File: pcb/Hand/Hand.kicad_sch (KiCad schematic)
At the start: 38 parts, among them J1 Conn_01x08_IMU_1, J10 Conn_01x03_HALL_7, J11 Conn_01x03_HALL_8, J12 Conn_01x03_HALL_9, J13 Conn_01x03_HALL_10, J14 Conn_01x03_HALL_11, J15 Conn_01x03_HALL_12, J16 Conn_01x03_HALL_13, J17 Conn_01x03_HALL_14, J18 Conn_01x03_HALL_15, J19 Conn_01x05_HAPTIC_1, J2 Conn_01x03_HALL_0, J20 Conn_01x05_HAPTIC_2, J21 Conn_01x05_HAPTIC_3, J22 Conn_01x05_HAPTIC_4, J23 Conn_01x03_FEEDBACK_0, J24 Conn_01x03_FEEDBACK_1, J25 Conn_01x03_FEEDBACK_2, J26 Conn_01x03_FEEDBACK_3, J27 Conn_01x03_FEEDBACK_4, J28 Conn_01x03_SPOOLPOT_1, J29 Conn_01x03_SPOOLPOT_2, J3 Conn_01x05_HAPTIC_0, J30 Conn_01x03_SPOOLPOT_3, J31 Conn_01x03_SPOOLPOT_0, J32 Conn_01x03_SPOOLPOT_4, J33 Conn_01x16_Ribbon_Bottom, J34 Conn_01x16_Ribbon_Top, J4 Conn_01x03_HALL_1, J5 Conn_01x03_HALL_2, J6 Conn_01x03_HALL_3, J7 Conn_01x03_HALL_4, J8 Conn_01x03_HALL_5, J9 Conn_01x03_HALL_6, U1 CD74HC4067M96, U3 TCA9548A

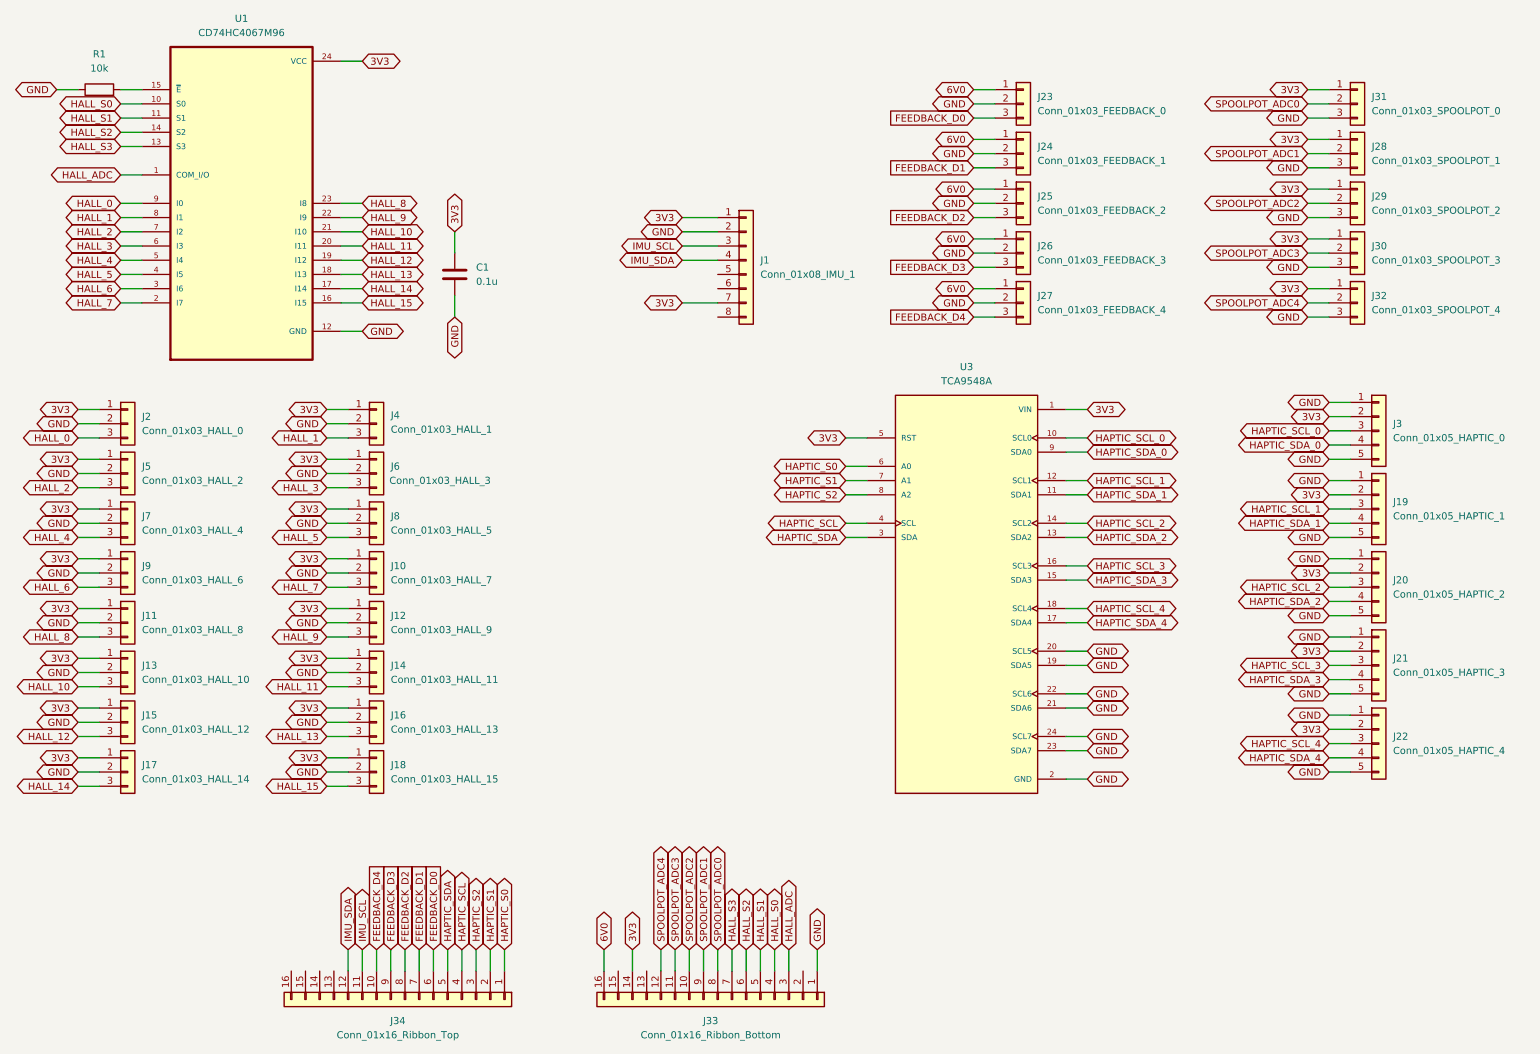
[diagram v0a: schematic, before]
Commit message: merging jackson pcb into main
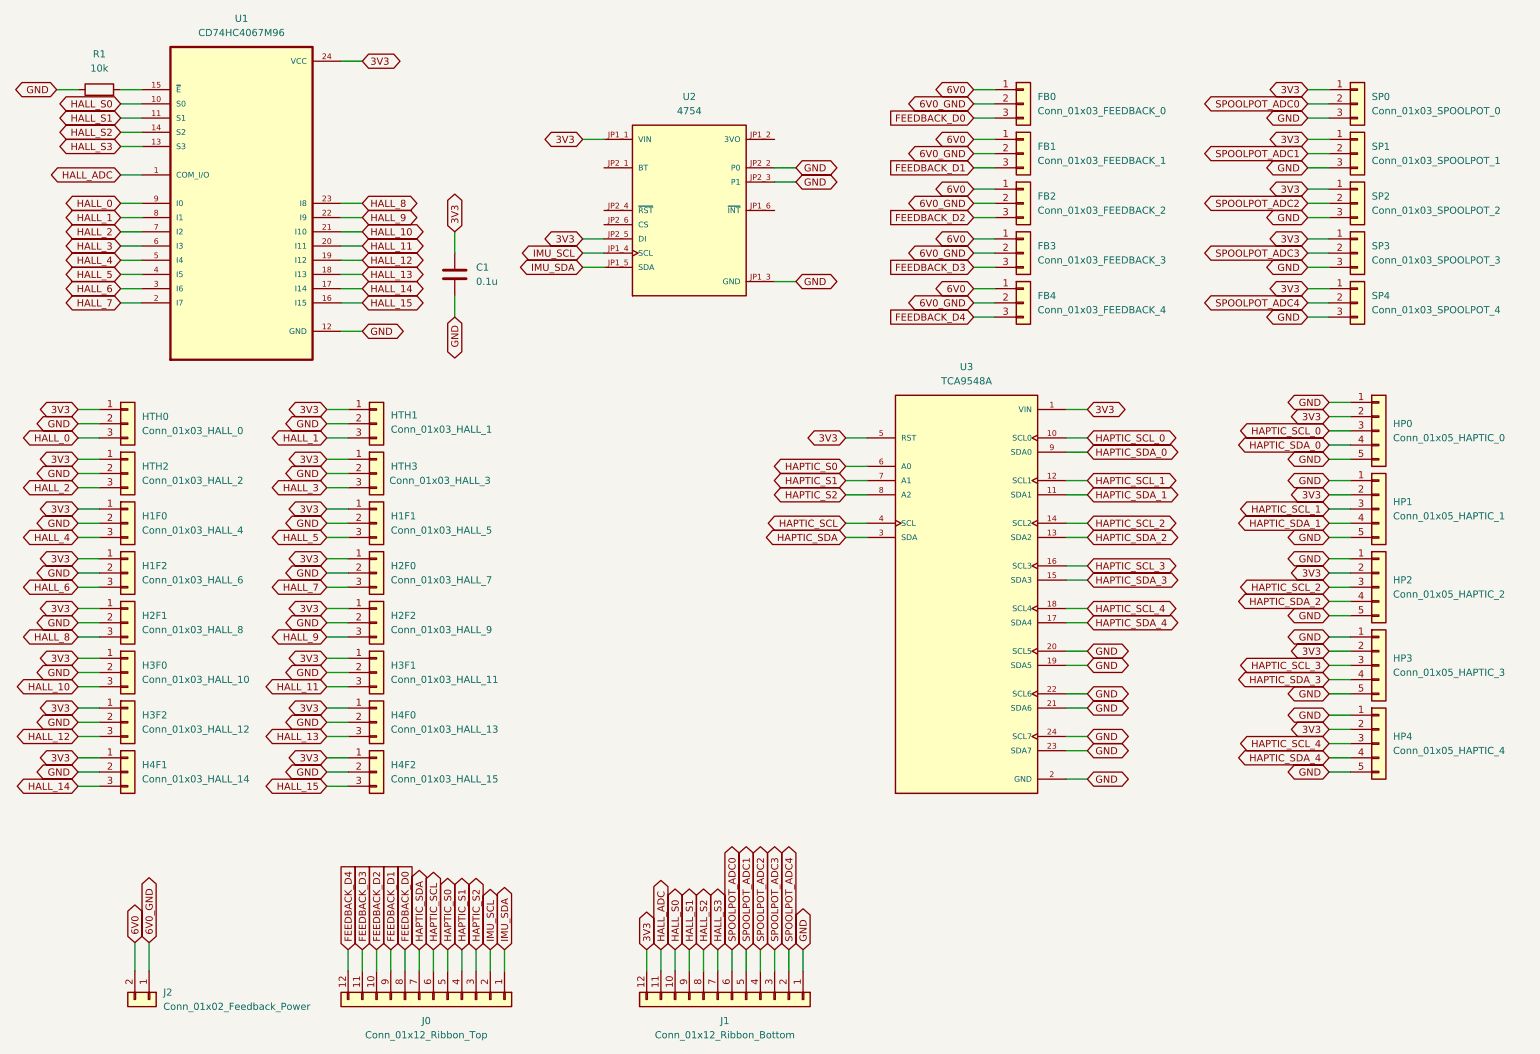
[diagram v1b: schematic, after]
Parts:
- removed J1: Conn_01x08_IMU_1, symbol Connector_Generic:Conn_01x08
- removed J33: Conn_01x16_Ribbon_Bottom, symbol Connector_Generic:Conn_01x16
- removed J34: Conn_01x16_Ribbon_Top, symbol Connector_Generic:Conn_01x16
- added J0: Conn_01x12_Ribbon_Top, 0522071233:0522071233, symbol Connector_Generic:Conn_01x12
- added J1: Conn_01x12_Ribbon_Bottom, 0522071233:0522071233, symbol Connector_Generic:Conn_01x12
- added J2: Conn_01x02_Feedback_Power, Connector_PinHeader_2.54mm:PinHeader_1x02_P2.54mm_Vertical, symbol Connector_Generic:Conn_01x02
- added U2: 4754, BNO085:MODULE_4754, symbol BNO085:4754
- C1: footprint (none) -> Capacitor_SMD:C_1206_3216Metric
- FB0: renamed from J23; footprint (none) -> SM03B-SRSS-TB:JST_SM03B-SRSS-TB_LF__SN_
- FB1: renamed from J24; footprint (none) -> SM03B-SRSS-TB:JST_SM03B-SRSS-TB_LF__SN_
- FB2: renamed from J25; footprint (none) -> SM03B-SRSS-TB:JST_SM03B-SRSS-TB_LF__SN_
- FB3: renamed from J26; footprint (none) -> SM03B-SRSS-TB:JST_SM03B-SRSS-TB_LF__SN_
- FB4: renamed from J27; footprint (none) -> SM03B-SRSS-TB:JST_SM03B-SRSS-TB_LF__SN_
- H1F0: renamed from J7; footprint (none) -> SM03B-SRSS-TB:JST_SM03B-SRSS-TB_LF__SN_
- H1F1: renamed from J8; footprint (none) -> SM03B-SRSS-TB:JST_SM03B-SRSS-TB_LF__SN_
- H1F2: renamed from J9; footprint (none) -> SM03B-SRSS-TB:JST_SM03B-SRSS-TB_LF__SN_
- H2F0: renamed from J10; footprint (none) -> SM03B-SRSS-TB:JST_SM03B-SRSS-TB_LF__SN_
- H2F1: renamed from J11; footprint (none) -> SM03B-SRSS-TB:JST_SM03B-SRSS-TB_LF__SN_
- H2F2: renamed from J12; footprint (none) -> SM03B-SRSS-TB:JST_SM03B-SRSS-TB_LF__SN_
- H3F0: renamed from J13; footprint (none) -> SM03B-SRSS-TB:JST_SM03B-SRSS-TB_LF__SN_
- H3F1: renamed from J14; footprint (none) -> SM03B-SRSS-TB:JST_SM03B-SRSS-TB_LF__SN_
- H3F2: renamed from J15; footprint (none) -> SM03B-SRSS-TB:JST_SM03B-SRSS-TB_LF__SN_
- H4F0: renamed from J16; footprint (none) -> SM03B-SRSS-TB:JST_SM03B-SRSS-TB_LF__SN_
- H4F1: renamed from J17; footprint (none) -> SM03B-SRSS-TB:JST_SM03B-SRSS-TB_LF__SN_
- H4F2: renamed from J18; footprint (none) -> SM03B-SRSS-TB:JST_SM03B-SRSS-TB_LF__SN_
- HP0: renamed from J3; footprint (none) -> SM05B-SRSS-TB:JST_SM05B-SRSS-TB_LF__SN_
- HP1: renamed from J19; footprint (none) -> SM05B-SRSS-TB:JST_SM05B-SRSS-TB_LF__SN_
- HP2: renamed from J20; footprint (none) -> SM05B-SRSS-TB:JST_SM05B-SRSS-TB_LF__SN_
- HP3: renamed from J21; footprint (none) -> SM05B-SRSS-TB:JST_SM05B-SRSS-TB_LF__SN_
- HP4: renamed from J22; footprint (none) -> SM05B-SRSS-TB:JST_SM05B-SRSS-TB_LF__SN_
- HTH0: renamed from J2; footprint (none) -> SM03B-SRSS-TB:JST_SM03B-SRSS-TB_LF__SN_
- HTH1: renamed from J4; footprint (none) -> SM03B-SRSS-TB:JST_SM03B-SRSS-TB_LF__SN_
- HTH2: renamed from J5; footprint (none) -> SM03B-SRSS-TB:JST_SM03B-SRSS-TB_LF__SN_
- HTH3: renamed from J6; footprint (none) -> SM03B-SRSS-TB:JST_SM03B-SRSS-TB_LF__SN_
- R1: footprint (none) -> Resistor_SMD:R_0402_1005Metric
- SP0: renamed from J31; footprint (none) -> SM03B-SRSS-TB:JST_SM03B-SRSS-TB_LF__SN_
- SP1: renamed from J28; footprint (none) -> SM03B-SRSS-TB:JST_SM03B-SRSS-TB_LF__SN_
- SP2: renamed from J29; footprint (none) -> SM03B-SRSS-TB:JST_SM03B-SRSS-TB_LF__SN_
- SP3: renamed from J30; footprint (none) -> SM03B-SRSS-TB:JST_SM03B-SRSS-TB_LF__SN_
- SP4: renamed from J32; footprint (none) -> SM03B-SRSS-TB:JST_SM03B-SRSS-TB_LF__SN_
- U3: footprint 2717:MODULE_2717 -> TCA9548A:MODULE_2717
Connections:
- net 3V3: now also J1.12 (Pin_12), U2.JP1_1 (VIN), U2.JP2_5 (DI)
- net 6V0: now also J2.2 (Pin_2)
- net FEEDBACK_D0: now also J0.8 (Pin_8)
- net FEEDBACK_D1: now also J0.9 (Pin_9)
- net FEEDBACK_D2: now also J0.10 (Pin_10)
- net FEEDBACK_D3: now also J0.11 (Pin_11)
- net FEEDBACK_D4: now also J0.12 (Pin_12)
- net GND: now also J1.1 (Pin_1), U2.JP1_3 (GND), U2.JP2_2 (P0), U2.JP2_3 (P1); no longer FB0.2 (Pin_2), FB1.2 (Pin_2), FB2.2 (Pin_2), FB3.2 (Pin_2), FB4.2 (Pin_2)
- net HALL_ADC: now also J1.11 (Pin_11)
- net HALL_S0: now also J1.10 (Pin_10)
- net HALL_S1: now also J1.9 (Pin_9)
- net HALL_S2: now also J1.8 (Pin_8)
- net HALL_S3: now also J1.7 (Pin_7)
- net HAPTIC_S0: now also J0.5 (Pin_5)
- net HAPTIC_S1: now also J0.4 (Pin_4)
- net HAPTIC_S2: now also J0.3 (Pin_3)
- net HAPTIC_SCL: now also J0.6 (Pin_6)
- net HAPTIC_SDA: now also J0.7 (Pin_7)
- net IMU_SCL: now also J0.2 (Pin_2), U2.JP1_4 (SCL)
- net IMU_SDA: now also J0.1 (Pin_1), U2.JP1_5 (SDA)
- net SPOOLPOT_ADC0: now also J1.6 (Pin_6)
- net SPOOLPOT_ADC1: now also J1.5 (Pin_5)
- net SPOOLPOT_ADC2: now also J1.4 (Pin_4)
- net SPOOLPOT_ADC3: now also J1.3 (Pin_3)
- net SPOOLPOT_ADC4: now also J1.2 (Pin_2)
- new net 6V0_GND: FB0.2 (Pin_2), FB1.2 (Pin_2), FB2.2 (Pin_2), FB3.2 (Pin_2), FB4.2 (Pin_2), J2.1 (Pin_1)

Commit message: revised pcbs in preparation for pcb review; added pull-ups etc to forearm
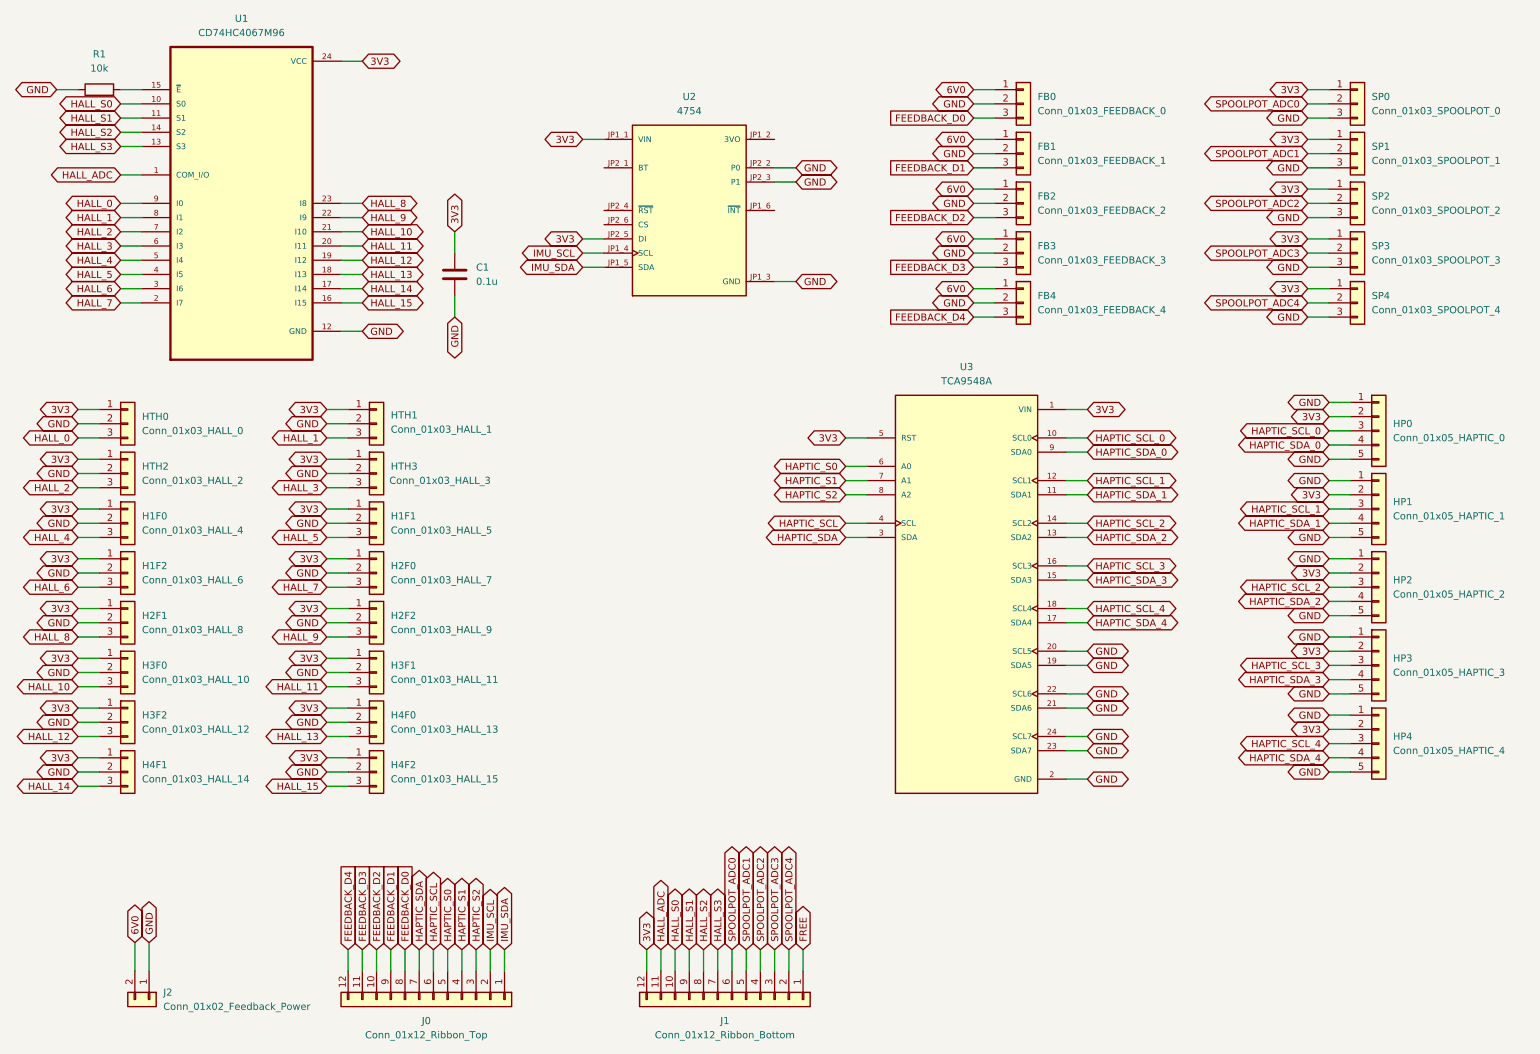
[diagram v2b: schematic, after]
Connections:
- net 6V0_GND is gone; now on net GND: FB0.2 (Pin_2), FB1.2 (Pin_2), FB2.2 (Pin_2), FB3.2 (Pin_2), FB4.2 (Pin_2), J2.1 (Pin_1)
- net GND: no longer J1.1 (Pin_1)
- new net FREE: J1.1 (Pin_1)
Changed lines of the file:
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@@
 	(global_label "GND"
 		(shape bidirectional)
+		(at 186.69 46.99 180)
+		(fields_autoplaced yes)
+		(effects
+			(font
+				(size 1.27 1.27)
+			)
+			(justify right)
+		)
+		(property "Intersheetrefs" "${INTERSHEET_REFS}"
+			(at 178.723 46.99 0)
+			(effects
+				(font
+					(size 1.27 1.27)
+				)
+				(justify right)
+				(hide yes)
+			)
+		)
+	)
+	(global_label "GND"
+		(shape bidirectional)
 		(at 71.12 148.59 180)
 		(fields_autoplaced yes)
@@
 		)
 	)
-	(global_label "GND"
+	(global_label "FREE"
 		(shape bidirectional)
 		(at 156.21 180.34 90)
@@
 		)
 		(property "Intersheetrefs" "${INTERSHEET_REFS}"
-			(at 156.21 172.373 90)
+			(at 156.21 171.5869 90)
 			(effects
 				(font
@@
 		)
 	)
-	(global_label "6V0_GND"
-		(shape bidirectional)
-		(at 186.69 38.1 180)
-		(fields_autoplaced yes)
-		(effects
-			(font
-				(size 1.27 1.27)
-			)
-			(justify right)
-		)
-		(property "Intersheetrefs" "${INTERSHEET_REFS}"
-			(at 174.2478 38.1 0)
-			(effects
-				(font
-					(size 1.27 1.27)
-				)
-				(justify right)
-				(hide yes)
-			)
-		)
-	)
 	(global_label "3V3"
 		(shape bidirectional)
@@
 		)
 	)
+	(global_label "GND"
+		(shape bidirectional)
+		(at 186.69 64.77 180)
+		(fields_autoplaced yes)
+		(effects
+			(font
+				(size 1.27 1.27)
+			)
+			(justify right)
+		)
+		(property "Intersheetrefs" "${INTERSHEET_REFS}"
+			(at 178.723 64.77 0)
+			(effects
+				(font
+					(size 1.27 1.27)
+				)
+				(justify right)
+				(hide yes)
+			)
+		)
+	)
 	(global_label "HAPTIC_SCL_0"
 		(shape bidirectional)
@@
 		)
 	)
-	(global_label "6V0_GND"
-		(shape bidirectional)
-		(at 39.37 179.07 90)
-		(fields_autoplaced yes)
-		(effects
-			(font
-				(size 1.27 1.27)
-			)
-			(justify left)
-		)
-		(property "Intersheetrefs" "${INTERSHEET_REFS}"
-			(at 39.37 166.6278 90)
-			(effects
-				(font
-					(size 1.27 1.27)
-				)
-				(justify left)
-				(hide yes)
-			)
-		)
-	)
 	(global_label "HALL_S3"
 		(shape bidirectional)
@@
 		)
 	)
-	(global_label "6V0_GND"
-		(shape bidirectional)
-		(at 186.69 46.99 180)
-		(fields_autoplaced yes)
-		(effects
-			(font
-				(size 1.27 1.27)
-			)
-			(justify right)
-		)
-		(property "Intersheetrefs" "${INTERSHEET_REFS}"
-			(at 174.2478 46.99 0)
-			(effects
-				(font
-					(size 1.27 1.27)
-				)
-				(justify right)
-				(hide yes)
-			)
-		)
-	)
 	(global_label "GND"
 		(shape bidirectional)
@@
 		)
 	)
-	(global_label "3V3"
+	(global_label "GND"
 		(shape bidirectional)
-		(at 246.38 26.67 180)
+		(at 39.37 179.07 90)
 		(fields_autoplaced yes)
 		(effects
@@
 				(size 1.27 1.27)
 			)
-			(justify right)
+			(justify left)
 		)
 		(property "Intersheetrefs" "${INTERSHEET_REFS}"
-			(at 238.7759 26.67 0)
+			(at 39.37 171.103 90)
 			(effects
 				(font
 					(size 1.27 1.27)
 				)
-				(justify right)
+				(justify left)
 				(hide yes)
 			)
 		)
 	)
-	(global_label "6V0_GND"
+	(global_label "3V3"
 		(shape bidirectional)
-		(at 186.69 55.88 180)
+		(at 246.38 26.67 180)
 		(fields_autoplaced yes)
 		(effects
@@
 		)
 		(property "Intersheetrefs" "${INTERSHEET_REFS}"
-			(at 174.2478 55.88 0)
+			(at 238.7759 26.67 0)
 			(effects
 				(font
@@
 		)
 	)
-	(global_label "6V0_GND"
-		(shape bidirectional)
-		(at 186.69 64.77 180)
-		(fields_autoplaced yes)
-		(effects
-			(font
-				(size 1.27 1.27)
-			)
-			(justify right)
-		)
-		(property "Intersheetrefs" "${INTERSHEET_REFS}"
-			(at 174.2478 64.77 0)
-			(effects
-				(font
-					(size 1.27 1.27)
-				)
-				(justify right)
-				(hide yes)
-			)
-		)
-	)
 	(global_label "6V0"
 		(shape bidirectional)
@@
 		)
 	)
-	(global_label "6V0_GND"
+	(global_label "HALL_14"
 		(shape bidirectional)
-		(at 186.69 29.21 180)
+		(at 26.67 151.13 180)
 		(fields_autoplaced yes)
 		(effects
@@
 		)
 		(property "Intersheetrefs" "${INTERSHEET_REFS}"
-			(at 174.2478 29.21 0)
+			(at 14.7116 151.13 0)
 			(effects
 				(font
@@
 		)
 	)
-	(global_label "HALL_14"
+	(global_label "GND"
 		(shape bidirectional)
-		(at 26.67 151.13 180)
+		(at 186.69 55.88 180)
 		(fields_autoplaced yes)
 		(effects
@@
 		)
 		(property "Intersheetrefs" "${INTERSHEET_REFS}"
-			(at 14.7116 151.13 0)
+			(at 178.723 55.88 0)
 			(effects
 				(font
@@
 	(global_label "GND"
 		(shape bidirectional)
+		(at 186.69 38.1 180)
+		(fields_autoplaced yes)
+		(effects
+			(font
+				(size 1.27 1.27)
+			)
+			(justify right)
+		)
+		(property "Intersheetrefs" "${INTERSHEET_REFS}"
+			(at 178.723 38.1 0)
+			(effects
+				(font
+					(size 1.27 1.27)
+				)
+				(justify right)
+				(hide yes)
+			)
+		)
+	)
+	(global_label "GND"
+		(shape bidirectional)
 		(at 26.67 139.7 180)
 		(fields_autoplaced yes)
@@
 				(hide yes)
 			)
+		)
+	)
+	(global_label "GND"
+		(shape bidirectional)
+		(at 186.69 29.21 180)
+		(fields_autoplaced yes)
+		(effects
+			(font
+				(size 1.27 1.27)
+			)
+			(justify right)
+		)
+		(property "Intersheetrefs" "${INTERSHEET_REFS}"
+			(at 178.723 29.21 0)
+			(effects
+				(font
+					(size 1.27 1.27)
+				)
+				(justify right)
+				(hide yes)
+			)

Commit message: revised pcbs in prep for manufacture, rev2
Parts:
- removed J0: Conn_01x12_Ribbon_Top, 0522071233:0522071233, symbol Connector_Generic:Conn_01x12
- removed J1: Conn_01x12_Ribbon_Bottom, 0522071233:0522071233, symbol Connector_Generic:Conn_01x12
- added J3: Conn_01x16_Top, 522071633:CON_522071633_MOL, symbol Connector_Generic:Conn_01x16
- added J4: Conn_01x16_Bottom, 522071633:CON_522071633_MOL, symbol Connector_Generic:Conn_01x16
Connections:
- net 3V3: now also J4.16 (Pin_16)
- net FEEDBACK_D0: now also J3.12 (Pin_12)
- net FEEDBACK_D1: now also J3.13 (Pin_13)
- net FEEDBACK_D2: now also J3.14 (Pin_14)
- net FEEDBACK_D3: now also J3.15 (Pin_15)
- net FEEDBACK_D4: now also J3.16 (Pin_16)
- net HALL_ADC: now also J4.15 (Pin_15)
- net HALL_S0: now also J4.14 (Pin_14)
- net HALL_S1: now also J4.13 (Pin_13)
- net HALL_S2: now also J4.12 (Pin_12)
- net HALL_S3: now also J4.11 (Pin_11)
- net HAPTIC_S0: now also J3.11 (Pin_11)
- net HAPTIC_S1: now also J3.10 (Pin_10)
- net HAPTIC_S2: now also J3.9 (Pin_9)
- net HAPTIC_SCL: now also J3.7 (Pin_7)
- net HAPTIC_SDA: now also J3.8 (Pin_8)
- net IMU_SCL: now also J3.6 (Pin_6)
- net IMU_SDA: now also J3.5 (Pin_5)
- net SPOOLPOT_ADC0: now also J4.10 (Pin_10)
- net SPOOLPOT_ADC1: now also J4.9 (Pin_9)
- net SPOOLPOT_ADC2: now also J4.8 (Pin_8)
- net SPOOLPOT_ADC3: now also J4.7 (Pin_7)
- net SPOOLPOT_ADC4: now also J4.6 (Pin_6)
- net IMU_1_INT: now reaches U2.JP1_6 (~{INT})
- net IMU_1_INT: now also J3.3 (Pin_3)
- net IMU_1_RST: now reaches U2.JP2_4 (~{RST})
- net IMU_1_RST: now also J3.4 (Pin_4)
